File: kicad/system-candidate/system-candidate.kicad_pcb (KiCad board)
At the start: 4 copper layers, 154 x 81 mm, 209 parts, among them J1 691137710002 2P 5.00mm, J2 Auxiliary 12V, J3 Differential audio, J301 T1_SECONDARY, J4 Control 2x4: 3V3 RESET FAULT 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, J401 START_BUTTON, J5 691137710002 2P 5.00mm, J6 GND braid solder bond - NO mo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, K501 G6K-2F DC12, Q501 MMBT3904, Q502 MMBT3904, U1 TPA3255DDV, U2 OPA1656ID, U3 OPA1656ID, U302 LM5164DDA, U303 TPS3700DDC, U401 LP2985-33, U402 TPS3808G33, U403 TPS3808G33, U404 TPS3808G33, U405 74LVC1G14, U406 74LVC2G74, U407 74LVC2G74, U408 74LVC1G32, U409 74LVC1G07, U410 74LVC1G08, U411 74LVC1G06, U412 TPS3700DDC, U413 TPS3700DDC, U414 TPS3808G33, U415 74LVC1G08, U416 TPS3808G33, U417 74LVC2G74, U418 74LVC1G32, U419 74LVC1G07, U501 TPS3700DDC, U502 TPS3700DDC, U503 TMUX6219, U504 TPS3700DDC

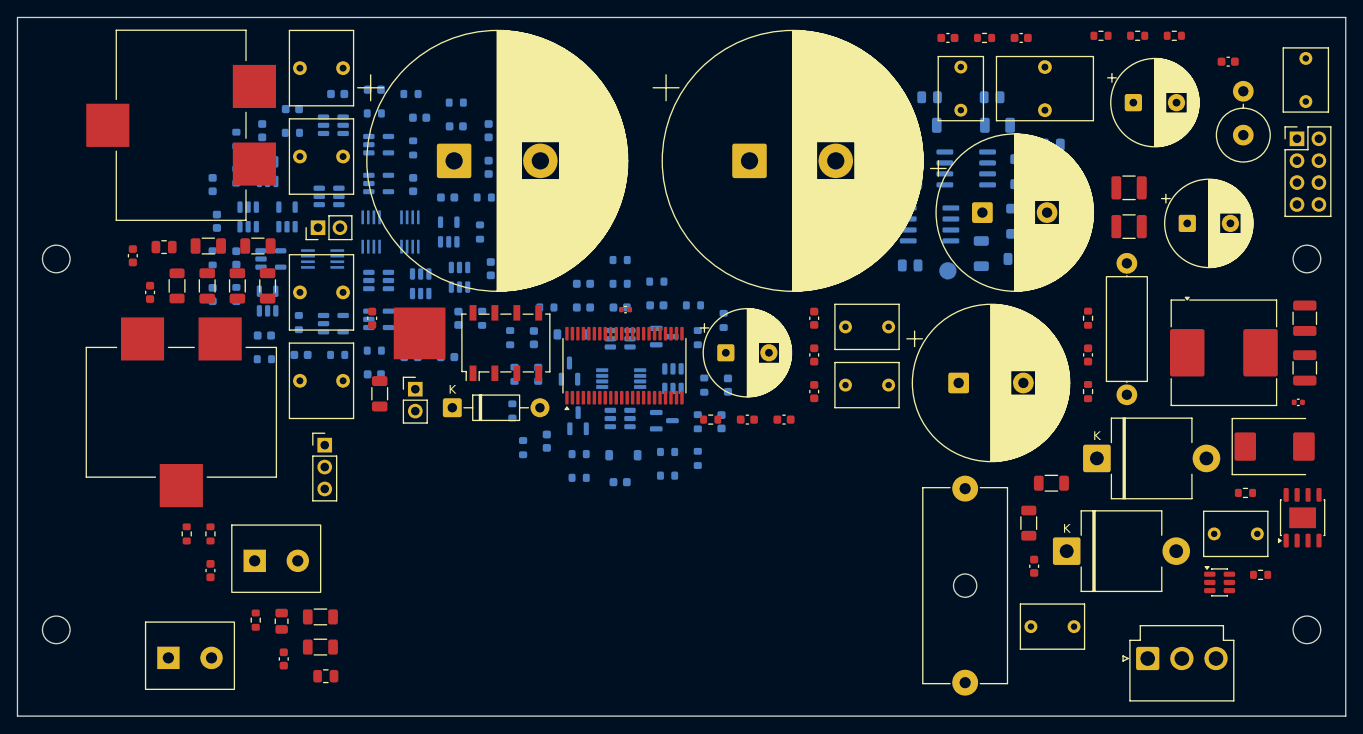
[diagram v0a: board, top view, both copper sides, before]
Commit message: feat(pcb): bloco térmico do TPA3255, J5 VH e medidas finais (D-031)
- medidas do proprietário: furos M3 roscados no perfil, perfil flutuante,
  polaridade do woofer e resistências de T1 (CT no pino central)
- placer: keepout do bloco térmico (só SMD baixo sob o bloco), J6 para trança GND
- J5 -> JST B2P-VH (chicote original do woofer); C14/C15 -> UHE1J681MHD D12,5,
  bulk PVDD 10,76 mF
- system-candidate regenerada: ERC 0, DRC 0, paridade 0, 471 conexões a rotear
- MECH-001 concluída; PCB-001 em andamento; gabarito 1:1 movido para FAB-001
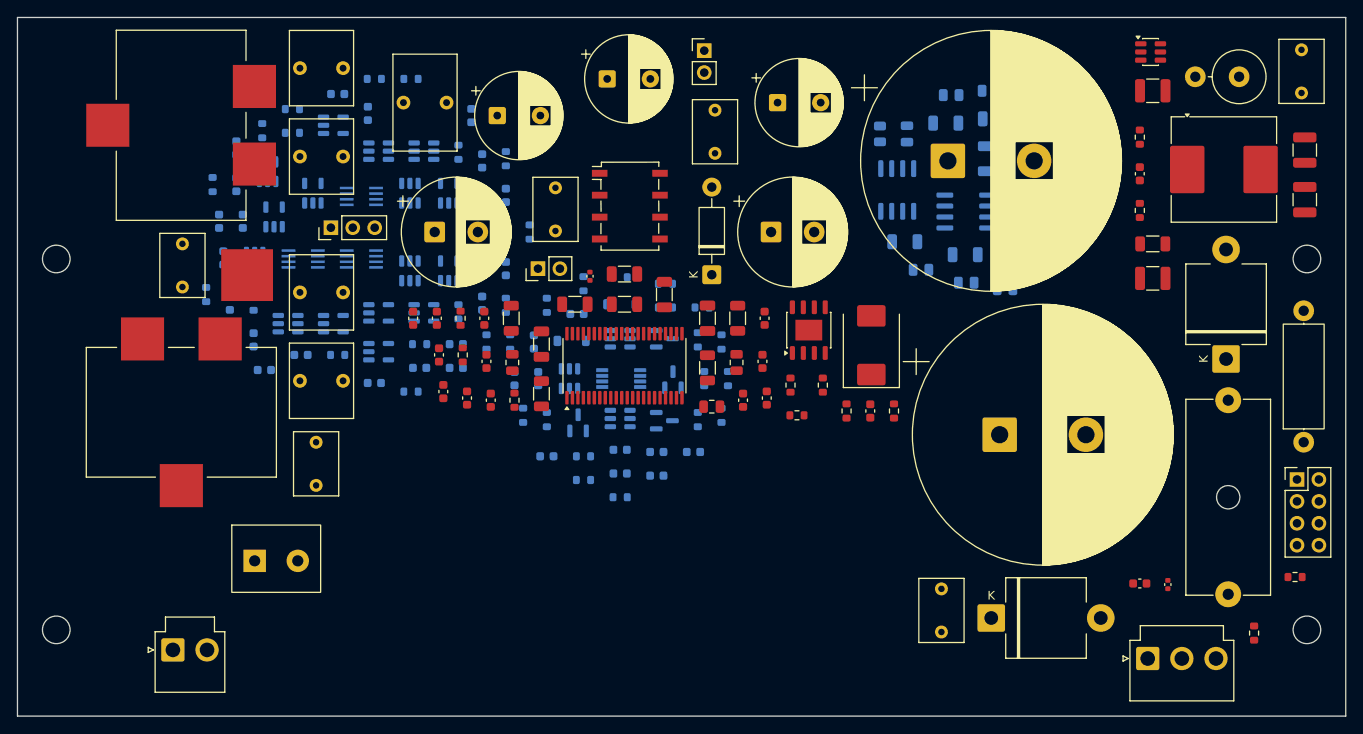
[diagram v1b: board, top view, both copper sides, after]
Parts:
- C14, C15: value 1500uF 63V -> 680uF 63V; footprint Capacitor_THT:CP_Radial_D18.0mm_P7.50mm -> Capacitor_THT:CP_Radial_D12.5mm_P5.00mm
- J5: value 691137710002 2P 5.00mm -> B2P-VH(LF)(SN); footprint PS28:WE_WR_TBL_691137710002 -> Connector_JST:JST_VH_B2P-VH_1x02_P3.96mm_Vertical
- moved C101 106.0 mm to (39.1, 51.2), turned to 90 degrees
- moved C102 104.3 mm to (54.6, 74.2), turned to 90 degrees
- moved C202 81.0 mm to (75.6, 31.4)
- moved C25 78.5 mm to (69.4, 63.4), turned to 90 degrees
- moved C103 74.6 mm to (127.1, 91.2)
- moved C203 74.4 mm to (64.8, 29.9), turned to 0 degrees
- moved R4 72.1 mm to (110.4, 66.1), turned to 0 degrees
- moved R310 71.5 mm to (163.4, 91.4), turned to 90 degrees
- moved R7 68.9 mm to (71.4, 54.9), turned to 90 degrees
- moved R3 67.7 mm to (109.6, 62.6)
- moved C21 66.1 mm to (100.5, 65.1)
- moved R6 64.5 mm to (77.2, 54.9)
- moved C14 63.2 mm to (68.4, 44.9)
- moved U303 62.0 mm to (151.4, 24.0)
- moved R1 61.6 mm to (103.5, 54.9), turned to 90 degrees
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
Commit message: feat(pcb): front-end OEM, placement final, bloco térmico e rota com planos
- D-032: preamp/limiter originais via J7 (JST XH 7 vias), ±15 V discretos,
  LIMIT por CLIP_OTW, ganho U2A 1,887; LR4 onboard removido
- placement revisado: LC junto do U1, buck sob L301, retificador do lado de T1
- bloco térmico: cotas, STL e modelo 3D (Blender); H5/H6 M3 em GND
- J5: modelo 3D JST B2P-VH feito no Blender
- cobre: planos GND/PVDD, fills, fanout do U1; 2.343 trilhas, 310 vias
- ERC 0, paridade 0; 56 conexões abertas e 4 starved_thermal pendentes
- ELEC-002/ELEC-004 concluídas; PCB-002 em andamento; nova task PCB-004
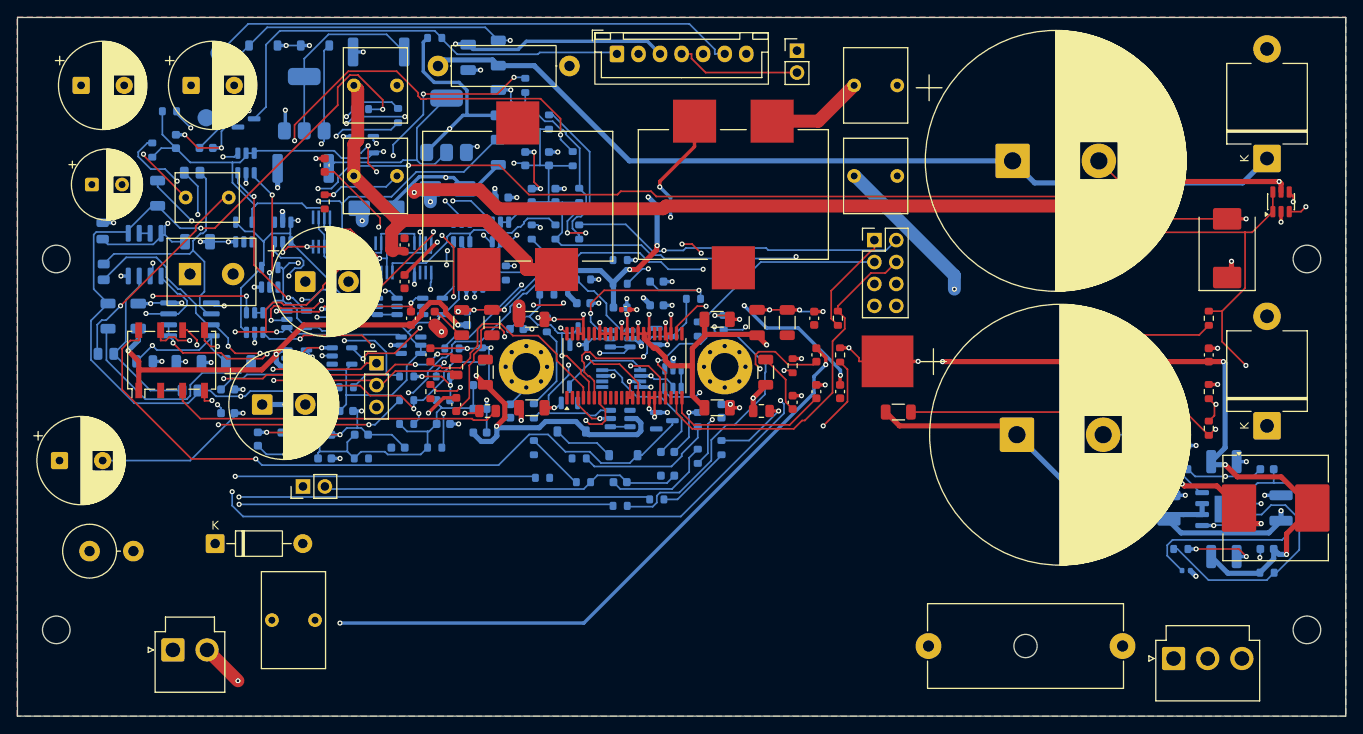
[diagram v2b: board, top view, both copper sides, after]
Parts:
- removed C101, C102, C103, C104, C105, C106: 100n, Capacitor_THT:C_Rect_L7.2mm_W5.0mm_P5.00mm
- removed R103, R104, R105, R106: 14k, Resistor_SMD:R_0805_2012Metric
- removed TP101: MONO_IN, TestPoint:TestPoint_Pad_D2.0mm
- added C109: 2.2u 63V film, Capacitor_THT:C_Rect_L7.2mm_W5.5mm_P5.00mm_FKS2_FKP2_MKS2_MKP2, F.Cu at (39.5, 40.9)
- added C601: 10u 25V, Capacitor_SMD:C_1206_3216Metric, B.Cu at (75.8, 29.9)
- added C602: 100n, Capacitor_SMD:C_0603_1608Metric, B.Cu at (41.9, 35.1)
- added C603: 120u 63V, Capacitor_THT:CP_Radial_D8.0mm_P3.50mm, F.Cu at (28.6, 39.4)
- added C604: 10u 25V, Capacitor_SMD:C_1206_3216Metric, B.Cu at (72.2, 24.6)
- added C605: 100n, Capacitor_SMD:C_0603_1608Metric, B.Cu at (58.9, 46.6)
- added D601: BZT52C16, Diode_SMD:D_SOD-123, B.Cu at (48.5, 23.2)
- added D602: S1M, Diode_SMD:D_SMA, B.Cu at (69.9, 39.9)
- added D603: S1M, Diode_SMD:D_SMA, B.Cu at (61.6, 42.1)
- added D604: BZT52C16, Diode_SMD:D_SOD-123, B.Cu at (54.5, 23.2)
- added H5: Thermal block clamp M3 (GND), MountingHole:MountingHole_3.2mm_M3_Pad_Via, F.Cu at (79.0, 60.5)
- added H6: Thermal block clamp M3 (GND), MountingHole:MountingHole_3.2mm_M3_Pad_Via, F.Cu at (102.0, 60.5)
- added J7: B7B-XH-A(LF)(SN), Connector_JST:JST_XH_B7B-XH-A_1x07_P2.50mm_Vertical, F.Cu at (89.5, 24.2)
- added Q601: BCP56, Package_TO_SOT_SMD:SOT-223-3_TabPin2, B.Cu at (69.8, 32.5)
- added Q602: BCP53, Package_TO_SOT_SMD:SOT-223-3_TabPin2, B.Cu at (53.2, 30.0)
- added Q603: BSS138, Package_TO_SOT_SMD:SOT-23, B.Cu at (46.5, 31.8)
- added R110: 8.87k, Resistor_SMD:R_0603_1608Metric, B.Cu at (64.1, 31.4)
- added R111: 10k, Resistor_SMD:R_0603_1608Metric, B.Cu at (59.9, 30.6)
- added R601: 470 1W, Resistor_SMD:R_2512_6332Metric, B.Cu at (53.1, 37.5)
- added R602: 10k, Resistor_SMD:R_1206_3216Metric, B.Cu at (75.8, 24.1)
- added R603: 470 1W, Resistor_SMD:R_2512_6332Metric, B.Cu at (61.9, 24.0)
- added R604: 10k, Resistor_SMD:R_1206_3216Metric, B.Cu at (75.8, 35.6)
- added R605: 10k, Resistor_SMD:R_0603_1608Metric, B.Cu at (68.4, 22.4)
- added TP102: STB, TestPoint:TestPoint_Pad_D2.0mm, B.Cu at (41.9, 31.6)
- added TP103: PTC, TestPoint:TestPoint_Pad_D2.0mm, B.Cu at (43.4, 24.1)
- C310, C311, C312, C313, C314, C315, C316, R310, R311, R312, R313, U302: moved to B.Cu
- R101: value 10k -> 1k
- R102: value 10k -> 100k
- moved R201 144.2 mm to (28.4, 81.9), turned to 0 degrees
- moved C107 109.5 mm to (29.9, 44.8)
- moved R301 109.4 mm to (68.8, 25.6), turned to 0 degrees
- moved R205 105.4 mm to (30.5, 54.6), turned to 90 degrees
- moved R101 104.5 mm to (30.2, 59.0)
- moved R202 102.8 mm to (34.0, 54.6)
- moved R108 94.8 mm to (30.0, 49.5), turned to 90 degrees
- moved C108 92.2 mm to (34.8, 59.9), turned to 0 degrees
- moved R203 91.9 mm to (40.9, 46.0), turned to 0 degrees
- moved R206 91.7 mm to (36.2, 40.4), turned to 90 degrees
- moved R207 90.9 mm to (39.9, 60.0)
- moved U3 90.9 mm to (40.0, 55.0)
- moved R107 90.7 mm to (40.2, 38.0)
- moved U2 87.6 mm to (34.8, 47.5)
- moved R102 85.4 mm to (40.0, 63.2), turned to 0 degrees
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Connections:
- net /FILTERED1 renamed /U2B_PARK
- R101 pad 1: MONO_BIASED -> /MONO_BIASED
- U2 pad 2: /BUFFERED -> /U2_FB
- U2 pad 5: /Y1 -> /VMID
- U3 pad 3: /Y2 -> /BUFFERED
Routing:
- net /GND: track 0.00 -> 948.1 mm, vias 0 -> 106
- net /AUX_RAW: track 0.00 -> 446.5 mm, vias 0 -> 20
- net /PVDD: track 0.00 -> 396.8 mm, vias 0 -> 9
- net /SEQ_3V3: track 0.00 -> 362.8 mm, vias 0 -> 8
- net /SPK_N: track 0.00 -> 249.4 mm, vias 0 -> 4
- net /RAILS_OK: track 0.00 -> 209.0 mm, vias 0 -> 5
- net /ANALOG_12V: track 0.00 -> 190.9 mm, vias 0 -> 5
- net /T1_A: track 0.00 -> 164.9 mm, vias 0 -> 1
- net /T1_B: track 0.00 -> 159.3 mm, vias 0 -> 3
- net /VMID: track 0.00 -> 155.3 mm, vias 0 -> 4
- net /RUN: track 0.00 -> 120.9 mm, vias 0 -> 4
- net /INB_DIS: track 0.00 -> 111.1 mm, vias 0 -> 4
- net /PWM_AC: track 0.00 -> 104.8 mm, vias 0 -> 3
- net /RESET: track 0.00 -> 102.8 mm, vias 0 -> 3
- net /INPUT_A_AC: track 0.00 -> 90.1 mm, vias 0 -> 2
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- added copper zone on B.Cu, net /GND
- added copper zone on F.Cu, net /GND
- added copper zone on In1.Cu, net /GND
- added copper zone on In2.Cu, net /PVDD
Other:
- board text added: "THERMAL BLOCK (mechanical/thermal-block.md)"

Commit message: feat(pcb): test points, LEDs de status, saída de fan e nova rota (PCB-004)
- 21 test points com nome no silk (SPK± fora), 6 LEDs: PVDD, RAILS_OK, RUN,
  AUDIO, FAULT, CLIP_OTW, só via gates de MOSFET
- fan 12 V em J8 com AO3400A, flyback e jumper de modo (sempre/CLIP_OTW)
- re-rota: 2.973 trilhas, 404 vias; ERC 0, paridade 0; 59 conexões abertas
  e 3 starved_thermal; removidos trechos PVDD/T1_A com isolamento 0,118 mm
- docs/bringup.md com valores esperados por test point; PCB-001/PCB-004 Done
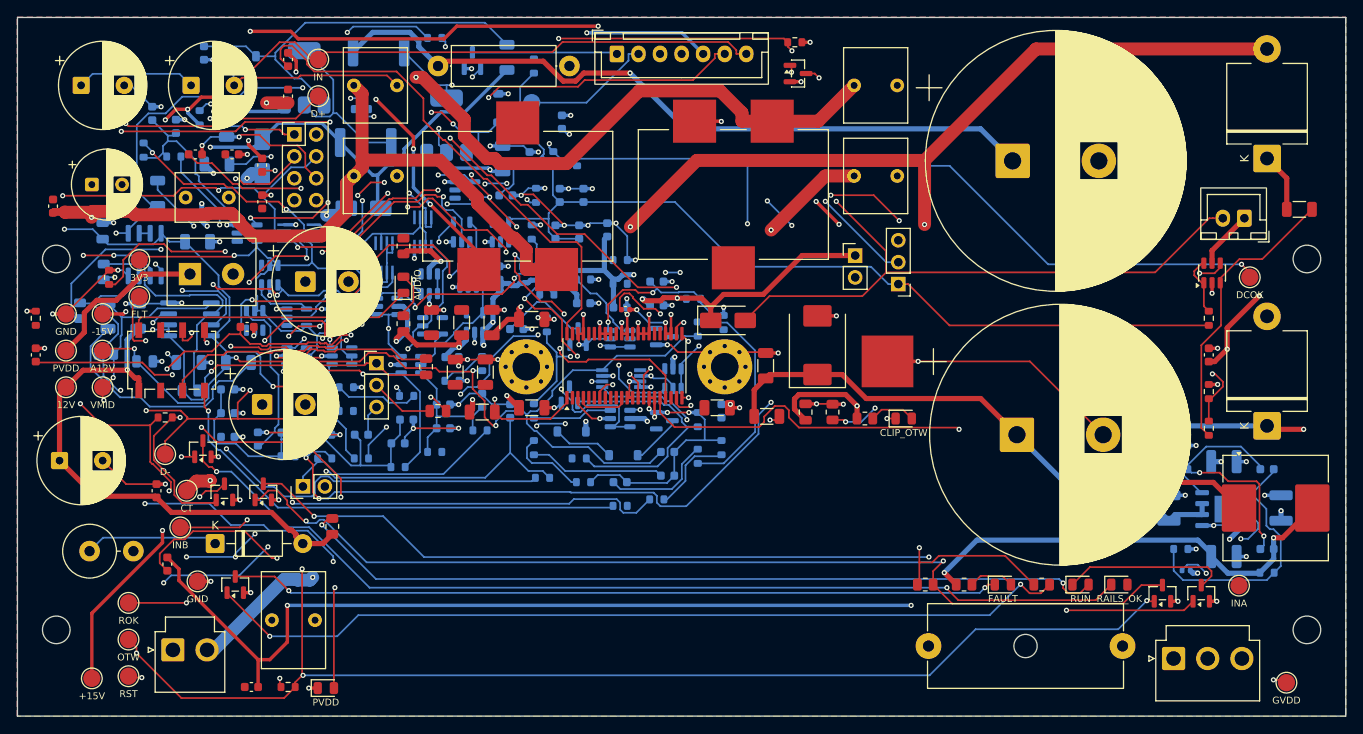
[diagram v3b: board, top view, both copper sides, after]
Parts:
- added D701: PVDD, LED_SMD:LED_0805_2012Metric, F.Cu at (55.8, 97.8)
- added D702: RAILS_OK, LED_SMD:LED_0805_2012Metric, F.Cu at (147.8, 85.8)
- added D703: RUN, LED_SMD:LED_0805_2012Metric, F.Cu at (143.2, 85.8)
- added D704: AUDIO, LED_SMD:LED_0805_2012Metric, F.Cu at (64.8, 51.0)
- added D705: FAULT, LED_SMD:LED_0805_2012Metric, F.Cu at (134.2, 85.8)
- added D706: CLIP_OTW, LED_SMD:LED_0805_2012Metric, F.Cu at (122.8, 66.5)
- added D707: S1M, Diode_SMD:D_SMA, F.Cu at (102.4, 55.1)
- added J8: FAN 12V, Connector_JST:JST_XH_B2B-XH-A_1x02_P2.50mm_Vertical, F.Cu at (162.2, 43.3)
- added JP701: FAN MODE, Connector_PinHeader_2.54mm:PinHeader_1x03_P2.54mm_Vertical, F.Cu at (122.1, 50.9)
- added Q701: BSS138, Package_TO_SOT_SMD:SOT-23, F.Cu at (41.5, 70.0)
- added Q702: BSS138, Package_TO_SOT_SMD:SOT-23, F.Cu at (157.2, 86.8)
- added Q703: BSS138, Package_TO_SOT_SMD:SOT-23, F.Cu at (44.0, 75.0)
- added Q704: BSS138, Package_TO_SOT_SMD:SOT-23, F.Cu at (45.2, 85.8)
- added Q705: BSS138, Package_TO_SOT_SMD:SOT-23, F.Cu at (152.8, 86.8)
- added Q706: BSS138, Package_TO_SOT_SMD:SOT-23, F.Cu at (48.5, 75.0)
- added Q707: AO3400A, Package_TO_SOT_SMD:SOT-23, F.Cu at (110.5, 26.5)
- added R701: 47k, Resistor_SMD:R_1206_3216Metric, F.Cu at (106.9, 66.2)
- added R702: 2.2k, Resistor_SMD:R_0805_2012Metric, F.Cu at (64.8, 46.5)
- added R703: 2.2k, Resistor_SMD:R_0805_2012Metric, F.Cu at (56.5, 79.0)
- added R704: 2.2k, Resistor_SMD:R_0805_2012Metric, F.Cu at (64.8, 55.5)
- added R705: 2.2k, Resistor_SMD:R_0805_2012Metric, F.Cu at (129.8, 85.8)
- added R706: 2.2k, Resistor_SMD:R_0805_2012Metric, F.Cu at (118.2, 66.5)
- added R715: 10k, Resistor_SMD:R_0805_2012Metric, F.Cu at (138.8, 85.8)
- added R716: 10k, Resistor_SMD:R_0805_2012Metric, F.Cu at (125.2, 85.8)
- added R720: 100k, Resistor_SMD:R_0805_2012Metric, F.Cu at (114.5, 65.8)
- added TP110: GND, TestPoint:TestPoint_Pad_D2.0mm, F.Cu at (25.6, 54.4)
- added TP111: PVDD, TestPoint:TestPoint_Pad_D2.0mm, F.Cu at (25.6, 58.6)
- added TP112: 12V, TestPoint:TestPoint_Pad_D2.0mm, F.Cu at (25.6, 62.9)
- added TP113: +15V, TestPoint:TestPoint_Pad_D2.0mm, F.Cu at (28.6, 96.6)
- added TP114: -15V, TestPoint:TestPoint_Pad_D2.0mm, F.Cu at (29.9, 54.4)
- added TP115: A12V, TestPoint:TestPoint_Pad_D2.0mm, F.Cu at (29.9, 58.6)
- added TP116: VMID, TestPoint:TestPoint_Pad_D2.0mm, F.Cu at (29.9, 62.9)
- added TP117: 3V3, TestPoint:TestPoint_Pad_D2.0mm, F.Cu at (34.1, 48.1)
- added TP118: GVDD, TestPoint:TestPoint_Pad_D2.0mm, F.Cu at (167.1, 97.1)
- added TP119: RST, TestPoint:TestPoint_Pad_D2.0mm, F.Cu at (32.9, 96.4)
- added TP120: FLT, TestPoint:TestPoint_Pad_D2.0mm, F.Cu at (34.1, 52.4)
- added TP121: OTW, TestPoint:TestPoint_Pad_D2.0mm, F.Cu at (32.9, 92.1)
- added TP122: ROK, TestPoint:TestPoint_Pad_D2.0mm, F.Cu at (32.9, 87.9)
- added TP123: DCOK, TestPoint:TestPoint_Pad_D2.0mm, F.Cu at (162.9, 50.1)
- added TP124: IN, TestPoint:TestPoint_Pad_D2.0mm, F.Cu at (54.9, 24.9)
- added TP125: D+, TestPoint:TestPoint_Pad_D2.0mm, F.Cu at (54.9, 29.1)
- added TP126: D-, TestPoint:TestPoint_Pad_D2.0mm, F.Cu at (37.1, 70.6)
- added TP127: INA, TestPoint:TestPoint_Pad_D2.0mm, F.Cu at (161.6, 85.9)
- added TP128: INB, TestPoint:TestPoint_Pad_D2.0mm, F.Cu at (38.9, 79.1)
- added TP129: CT, TestPoint:TestPoint_Pad_D2.0mm, F.Cu at (39.6, 74.9)
- added TP130: GND, TestPoint:TestPoint_Pad_D2.0mm, F.Cu at (40.9, 85.4)
- moved R3 85.2 mm to (30.6, 50.1)
- moved C5 77.1 mm to (40.6, 35.9), turned to 0 degrees
- moved R8 76.8 mm to (51.4, 97.6), turned to 0 degrees
- moved C17 76.4 mm to (47.1, 97.6), turned to 0 degrees
- moved C16 70.2 mm to (51.4, 24.9)
- moved J4 68.4 mm to (52.1, 33.6)
- moved C9 65.4 mm to (48.4, 41.4)
- moved C4 63.9 mm to (46.6, 55.9), turned to 0 degrees
- moved R320 52.1 mm to (168.6, 42.2)
- moved R407 49.1 mm to (55.6, 71.1), turned to 0 degrees
- moved D303 48.8 mm to (112.8, 58.0)
- moved C408 47.9 mm to (85.1, 44.9)
- moved C409 46.4 mm to (38.4, 32.6), turned to 90 degrees
- moved C413 45.9 mm to (44.4, 63.1), turned to 0 degrees
- moved R430 45.1 mm to (38.1, 36.1), turned to 0 degrees
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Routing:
- net /CLIP_OTW: track 42.2 -> 320.6 mm, vias 0 -> 8
- net /GVDD_AB: track 7.03 -> 225.4 mm, vias 0 -> 4
- net /CLIP_N: track 0.00 -> 155.3 mm, vias 0 -> 2
- net /DC_OK: track 37.7 -> 186.1 mm, vias 2 -> 10
- net /RESET: track 102.8 -> 249.8 mm, vias 3 -> 10
- net /P15V: track 59.3 -> 184.4 mm, vias 1 -> 6
- net /FAULT_N: track 0.00 -> 124.1 mm, vias 0 -> 3
- net /LED_ROK_K: track 0.00 -> 115.2 mm, vias 0 -> 2
- net /INB_DIS: track 111.1 -> 0.00 mm, vias 4 -> 0
- net /PWM_BD: track 77.0 -> 178.1 mm
- net /DIVIDED: track 19.9 -> 120.9 mm, vias 0 -> 4
- net /LED706_K: track 0.00 -> 99.8 mm, vias 0 -> 3
- net /T1_CT: track 35.0 -> 131.7 mm, vias 0 -> 1
- net /VIO_3V3_EXTERNAL: track 12.4 -> 108.5 mm, vias 0 -> 6
- net /LED703_A: track 0.00 -> 94.5 mm, vias 0 -> 2
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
